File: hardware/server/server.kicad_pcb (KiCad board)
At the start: 2 copper layers, 49.5 x 53.3 mm, 15 parts

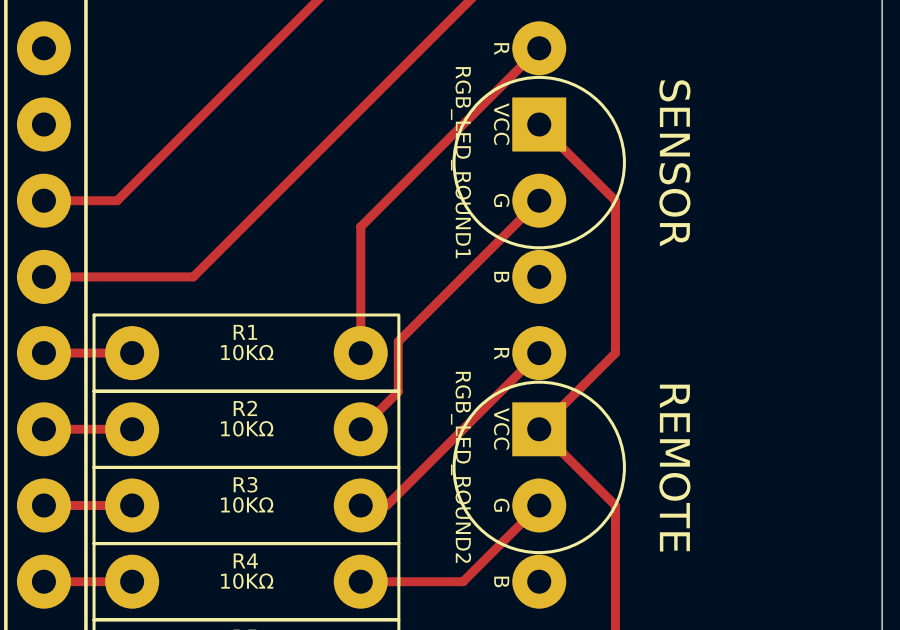
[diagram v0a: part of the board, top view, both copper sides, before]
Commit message: hardware: Update pcd design for better wiring clearance.
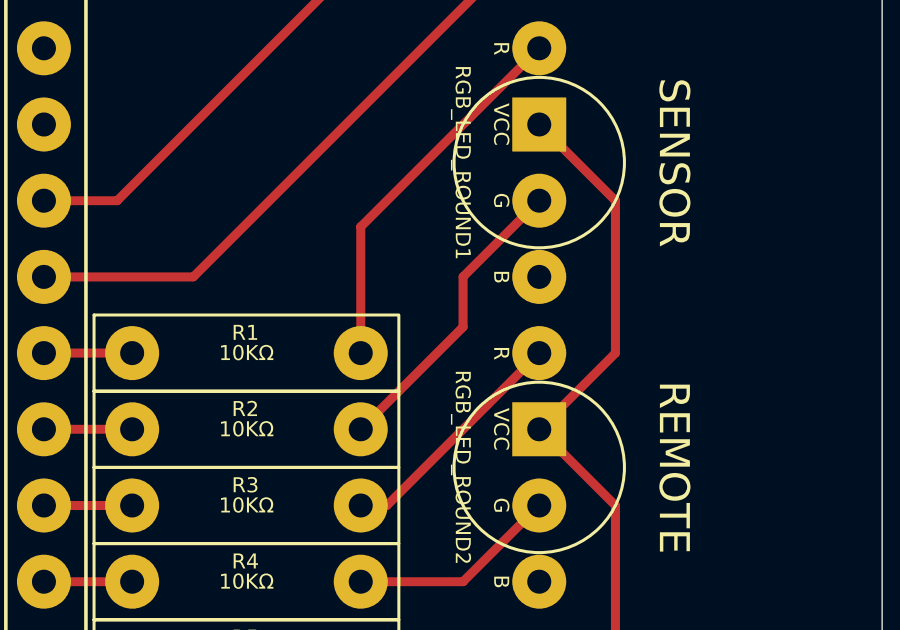
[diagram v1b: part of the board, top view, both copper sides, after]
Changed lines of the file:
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@@
 	)
 	(segment
-		(start 48.641 40.259)
-		(end 48.641 41.929)
+		(start 50.8 39.77)
+		(end 50.8 38.1)
 		(width 0.3)
 		(layer "F.Cu")
@@
 	)
 	(segment
-		(start 48.641 41.929)
-		(end 47.39 43.18)
+		(start 47.39 43.18)
+		(end 50.8 39.77)
 		(width 0.3)
 		(layer "F.Cu")
@@
 	)
 	(segment
-		(start 53.34 35.56)
-		(end 48.641 40.259)
+		(start 50.8 38.1)
+		(end 53.34 35.56)
 		(width 0.3)
 		(layer "F.Cu")

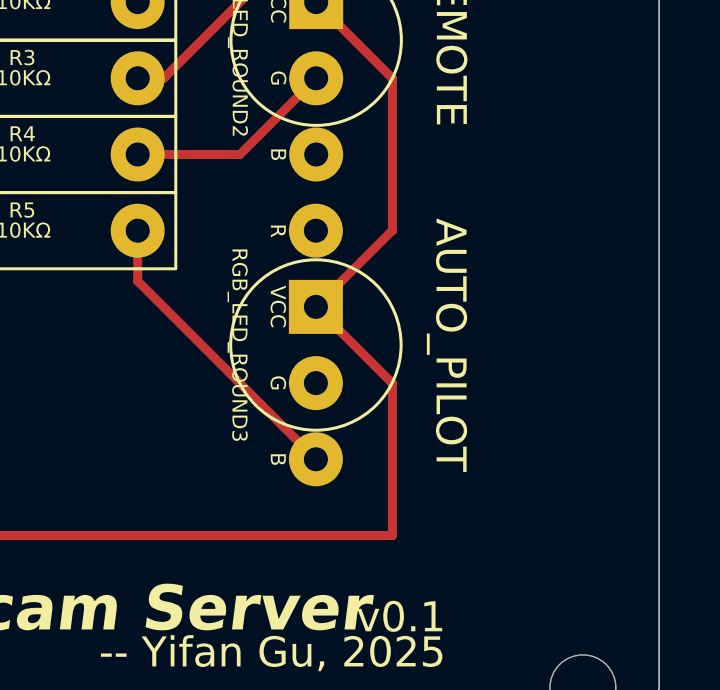
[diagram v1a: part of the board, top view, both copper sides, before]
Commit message: hardware: Revise the drive mode naming.
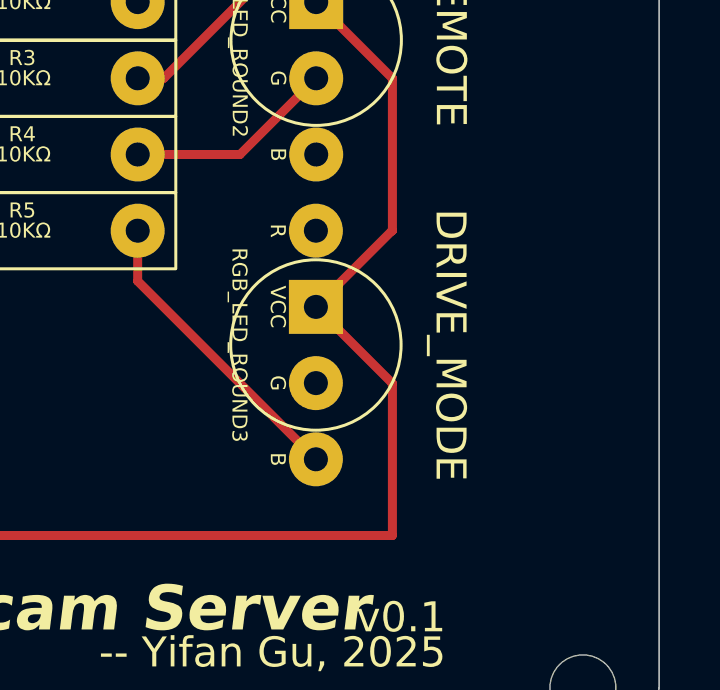
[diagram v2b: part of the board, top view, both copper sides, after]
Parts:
- RGB_LED_ROUND3: value AUTO_PILOT -> DRIVE_MODE
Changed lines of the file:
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@@
 			)
 		)
-		(property "Value" "AUTO_PILOT"
+		(property "Value" "DRIVE_MODE"
 			(at 0 -5.07 270)
 			(unlocked yes)
